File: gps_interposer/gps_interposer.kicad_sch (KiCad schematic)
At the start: 9 parts, among them J1 Module Connector, J2 Carrier Connector, J3 Conn_01x10, U1 SN74LVC1T45DBV, U2 SN74LVC1T45DBV

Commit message: PCB almost done.
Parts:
- removed J3: Conn_01x10, symbol Connector_Generic:Conn_01x10
- removed JP1: TXD, symbol Jumper:Jumper_2_Bridged
- added J3: Ext VSYS, Connector_PinHeader_2.54mm:PinHeader_1x02_P2.54mm_Horizontal, symbol Connector:Conn_01x02_Pin
- added J4: GENERIC_3V0, Connector_PinHeader_2.54mm:PinHeader_1x01_P2.54mm_Horizontal, symbol Connector_Generic:Conn_01x01
- added J6: GENERIC_3V3, Connector_PinHeader_2.54mm:PinHeader_1x01_P2.54mm_Horizontal, symbol Connector_Generic:Conn_01x01
- added JP1: TXD Direct, Connector_PinHeader_2.54mm:PinHeader_1x03_P2.54mm_Horizontal, symbol Jumper:Jumper_3_Bridged12
- added JP4: 3V3 Zero, Connector_PinHeader_2.54mm:PinHeader_1x02_P2.54mm_Horizontal, symbol Jumper:Jumper_2_Bridged
- added JP5: 1PPS Direct, Connector_PinHeader_2.54mm:PinHeader_1x02_P2.54mm_Horizontal, symbol Jumper:Jumper_2_Bridged
- added R10, R11, R17, R18, R20, R27, R3, R5, R7, R8: NC, Resistor_SMD:R_0603_1608Metric_Pad0.98x0.95mm_HandSolder, symbol Device:R
- added R12, R19, R21, R4, R6, R9: 1K, Resistor_SMD:R_0603_1608Metric_Pad0.98x0.95mm_HandSolder, symbol Device:R
- added R13, R14, R15, R16, R22, R23, R24, R25, R26: 0, Resistor_SMD:R_0603_1608Metric_Pad0.98x0.95mm_HandSolder, symbol Device:R
- added U3: RP20240-Zero, Kicad_Personal:RP2040-Zero, symbol Kicad_Personal:rp2040-zero
- added U4, U5, U6, U7: SN74LVC1T45DBV, Package_TO_SOT_SMD:SOT-23-6, symbol Logic_LevelTranslator:SN74LVC1T45DBV
- J1: footprint (none) -> Connector_PinSocket_1.27mm:PinSocket_2x05_P1.27mm_Vertical_SMD
- J2: value Carrier Connector -> Motherboard/Carrier Connector; footprint (none) -> Connector_PinHeader_1.27mm:PinHeader_2x05_P1.27mm_Vertical_SMD
- JP2: value Jumper_3_Bridged12 -> RXD Direct; footprint (none) -> Connector_PinHeader_2.54mm:PinHeader_1x03_P2.54mm_Horizontal
- R1, R2: value R -> NC; footprint (none) -> Resistor_SMD:R_0603_1608Metric_Pad0.98x0.95mm_HandSolder
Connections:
- net +3.3V: now also U2.6 (VCCB), JP4.1 (A), R8.2, U4.1 (VCCA), U5.6 (VCCB), U6.6 (VCCB), U7.6 (VCCB); no longer U2.1 (VCCA)
- net +3V0: now also U2.1 (VCCA), R11.2, R18.2, R21.2, R4.2, R5.2, U4.6 (VCCB), U5.1 (VCCA), U6.1 (VCCA), U7.1 (VCCA); no longer U2.6 (VCCB)
- net 1PPS_C: now also JP5.2 (B)
- net 1PPS_M: now also JP5.1 (A), R7.2, U4.4 (B)
- net ANT_BIAS_C: now also R25.2
- net ANT_BIAS_M: now also R25.1
- net BATT_C: now also R22.2
- net BATT_M: now also R22.1
- net GND: now also J3.1 (Pin_1), R12.1, R19.1, R27.1, R3.1, R6.1, R9.1, U3.22 (GND), U4.2 (GND), U5.2 (GND), U6.2 (GND), U7.2 (GND); no longer U1.5 (DIR), U2.5 (DIR)
- net RTCM_IN_C: now also R24.2
- net RTCM_IN_M: now also R24.1
- net RXD_C: now also JP2.2 (C), R20.2, U7.3 (A)
- net RXD_M_3V3: now also R13.2
- net TXD_C: now also JP1.2 (C)
- net TXD_M: now also U2.3 (A), JP1.1 (A); no longer U2.4 (B)
- net TXD_M_3V3: now also U2.4 (B), R14.2; no longer U2.3 (A)
- net RXD_M_3V0: now reaches JP2.3 (B), R2.1, U1.3 (A)
- net RSVD10 renamed RSVD10_C
- net RSVD10_C: now also R26.2; no longer J1.10 (Pin_10)
- net RSVD7 renamed RSVD7_C
- net RSVD7_C: now also R23.2; no longer J1.7 (Pin_7)
- new net: J4.1 (Pin_1), R17.1, U6.3 (A)
- new net: J6.1 (Pin_1), R17.2, U6.4 (B)
- new net: R21.1, R27.2, U7.5 (DIR)
- new net: R8.1, R9.2, U4.5 (DIR)
- new net: R13.1, U3.1 (GPIO0/SPI0_RX/I2C0_SDA/UART0_TX)
- new net: R14.1, U3.2 (GPIO1/SPI0_CSn/I2C0_SCL/UART0_RX)
- new net: JP4.2 (B), U3.21 (3V3)
- new net: J3.2 (Pin_2), U3.23 (VSYS)
- new net: R15.1, U3.5 (GPIO4/SPI0_RX_I2C0_SDA/UART1_TX)
- new net: R16.1, U3.6 (GPIO5/SPI0_CSn/I2C0_SCL/UART1_RX)
- new net: R5.1, R6.2, U1.5 (DIR)
- new net: R11.1, R12.2, U5.5 (DIR)
- new net: R3.2, R4.1, U2.5 (DIR)
- new net: R18.1, R19.2, U6.5 (DIR)
- new net 1PPS_M_3V3: R7.1, U3.3 (GPIO2/SPI0_SCLK/I2C1_SDA), U4.3 (A)
- new net RSVD10_M: J1.10 (Pin_10), R26.1
- new net RSVD7_M: J1.7 (Pin_7), R23.1
- new net RXD_C_3V3: R16.2, R20.1, U7.4 (B)
- new net TXD_C_3V0: JP1.3 (B), R10.1, U5.3 (A)
- new net TXD_C_3V3: R10.2, R15.2, U5.4 (B)
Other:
- note added: "---->"
- note added: "<----"
- note added: "DIR low -> B to A direction"
- moved on the sheet: J1, J2, JP2, R1, R2, U1

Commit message: PCB ready.
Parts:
- removed J4: GENERIC_3V0, Connector_PinHeader_2.54mm:PinHeader_1x01_P2.54mm_Horizontal, symbol Connector_Generic:Conn_01x01
- removed J6: GENERIC_3V3, Connector_PinHeader_2.54mm:PinHeader_1x01_P2.54mm_Horizontal, symbol Connector_Generic:Conn_01x01
- removed JP1: TXD Direct, Connector_PinHeader_2.54mm:PinHeader_1x03_P2.54mm_Horizontal, symbol Jumper:Jumper_3_Bridged12
- removed JP2: RXD Direct, Connector_PinHeader_2.54mm:PinHeader_1x03_P2.54mm_Horizontal, symbol Jumper:Jumper_3_Bridged12
- removed JP4: 3V3 Zero, Connector_PinHeader_2.54mm:PinHeader_1x02_P2.54mm_Horizontal, symbol Jumper:Jumper_2_Bridged
- removed JP5: 1PPS Direct, Connector_PinHeader_2.54mm:PinHeader_1x02_P2.54mm_Horizontal, symbol Jumper:Jumper_2_Bridged
- removed R17, R18: NC, Resistor_SMD:R_0603_1608Metric_Pad0.98x0.95mm_HandSolder, symbol Device:R
- removed R19: 1K, Resistor_SMD:R_0603_1608Metric_Pad0.98x0.95mm_HandSolder, symbol Device:R
- removed U6: SN74LVC1T45DBV, Package_TO_SOT_SMD:SOT-23-6, symbol Logic_LevelTranslator:SN74LVC1T45DBV
- added C1, C2, C4: 100n, Capacitor_SMD:C_0603_1608Metric_Pad1.08x0.95mm_HandSolder, symbol Device:C
- added H1, H2, H3, H4, H5, H6, H7, H8: MountingHole_Pad, Kicad_Personal:MountingHole_3.7mm_3.9mm_Pad_TopBottom, symbol Mechanical:MountingHole_Pad
- added R28, R30: NS, Resistor_SMD:R_0603_1608Metric_Pad0.98x0.95mm_HandSolder, symbol Device:R
- added R29, R31, R32, R33: 0, Resistor_SMD:R_0603_1608Metric_Pad0.98x0.95mm_HandSolder, symbol Device:R
- R2, R5: value NC -> NS
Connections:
- net +3.3V: now also R32.2
- net +3V0: now also C1.1, C2.1, C4.1
- net 1PPS_C: now also R33.2
- net 1PPS_M: now also R33.1
- net GND: now also C1.2, C2.2, C4.2, H1.1, H2.1, H3.1, H4.1, H5.1, H6.1, H7.1, H8.1
- net RXD_C: now also R29.2
- net RXD_M: now also R28.2, R29.1
- net RXD_M_3V0: now also R28.1
- net TXD_C: now also R30.2, R31.1
- net TXD_C_3V0: now also R30.1
- net TXD_M: now also R31.2
- net at U3.21 (3V3): now also R32.1

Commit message: PCB v2.
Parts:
- removed C1, C2, C4: 100n, Capacitor_SMD:C_0603_1608Metric_Pad1.08x0.95mm_HandSolder, symbol Device:C
- removed J3: Ext VSYS, Connector_PinHeader_2.54mm:PinHeader_1x02_P2.54mm_Horizontal, symbol Connector:Conn_01x02_Pin
- removed R1, R11, R20, R27, R3, R8: NC, Resistor_SMD:R_0603_1608Metric_Pad0.98x0.95mm_HandSolder, symbol Device:R
- removed R12, R21, R4, R6, R9: 1K, Resistor_SMD:R_0603_1608Metric_Pad0.98x0.95mm_HandSolder, symbol Device:R
- removed R22, R23, R24, R25, R26, R32, R33: 0, Resistor_SMD:R_0603_1608Metric_Pad0.98x0.95mm_HandSolder, symbol Device:R
- removed R28, R30, R5: NS, Resistor_SMD:R_0603_1608Metric_Pad0.98x0.95mm_HandSolder, symbol Device:R
- removed U1, U2, U4, U5, U7: SN74LVC1T45DBV, Package_TO_SOT_SMD:SOT-23-6, symbol Logic_LevelTranslator:SN74LVC1T45DBV
- added J5: Conn_01x04_Pin, Connector_PinHeader_2.54mm:PinHeader_1x04_P2.54mm_Horizontal, symbol Connector:Conn_01x04_Pin
- added R17, R18, R19: 9k, Resistor_SMD:R_0603_1608Metric_Pad0.98x0.95mm_HandSolder, symbol Device:R
- H1, H2, H3, H4, H5, H6, H7, H8: footprint Kicad_Personal:MountingHole_3.7mm_3.9mm_Pad_TopBottom -> Kicad_Personal:MountingHole_2.5mm_3.9mm_Pad_TopBottom_1
- R10: value NC -> 1k
- R13, R16, R31: now not fitted; now left out of the parts list
- R2: value NS -> 1k; now not fitted; now left out of the parts list
- R7: value NC -> 1k; now not fitted; now left out of the parts list
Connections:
- net ANT_BIAS_M is gone; now on net ANT_BIAS_C: J1.9 (Pin_9)
- net BATT_M is gone; now on net BATT_C: J1.6 (Pin_6)
- net RSVD10_M is gone; now on net RSVD10_C: J1.10 (Pin_10)
- net RSVD7_M is gone; now on net RSVD7_C: J1.7 (Pin_7)
- net RTCM_IN_M is gone; now on net RTCM_IN_C: J1.8 (Pin_8)
- net RXD_C_3V3 is gone; now on net RXD_C: R16.2
- net RXD_M_3V0 is gone; now on net RXD_M_3V3: R2.1
- net TXD_C_3V0 is gone; now on net TXD_C: R10.1
- net TXD_M_3V3 is gone; now on net TXD_M: R14.2
- net +3.3V: now also U3.21 (3V3), J5.2 (Pin_2)
- net +3V0: now also J5.1 (Pin_1)
- net 1PPS_C: now also J1.4 (Pin_4), R7.1
- net 1PPS_M_3V3: now also R7.2, R17.2; no longer R7.1
- net GND: now also J5.4 (Pin_4), R17.1, R18.1, R19.1
- net RTCM_IN_C: now also U3.10 (GPIO9/SPI1_CSn/I2C0_SCL/UART1_RX)
- net RXD_M: now also R2.2, R18.2
- net RXD_M_3V3: no longer R2.2
- net TXD_C: now also R19.2
- net VSYS: now reaches U3.23 (VSYS)
- net VSYS: now also J5.3 (Pin_3)
- removed net 1PPS_M: J1.4 (Pin_4), R7.2
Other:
- moved on the sheet: R10

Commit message: Additional connectors.
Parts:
- added J3: Conn_01x05, Connector_PinHeader_2.54mm:PinHeader_1x05_P2.54mm_Vertical_SMD_Pin1Left, symbol Connector_Generic:Conn_01x05
- added J4: Conn_01x04, Connector_PinHeader_2.54mm:PinHeader_1x04_P2.54mm_Horizontal, symbol Connector_Generic:Conn_01x04
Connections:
- net +3.3V: now also J4.1 (Pin_1)
- net 1PPS_C: now also J3.4 (Pin_4)
- net GND: now also J3.5 (Pin_5), J4.4 (Pin_4)
- net RXD_M: now also J3.1 (Pin_1)
- net TXD_C: now also J3.3 (Pin_3)
- net TXD_M: now also J3.2 (Pin_2)
- net VSYS: now also J4.2 (Pin_2)

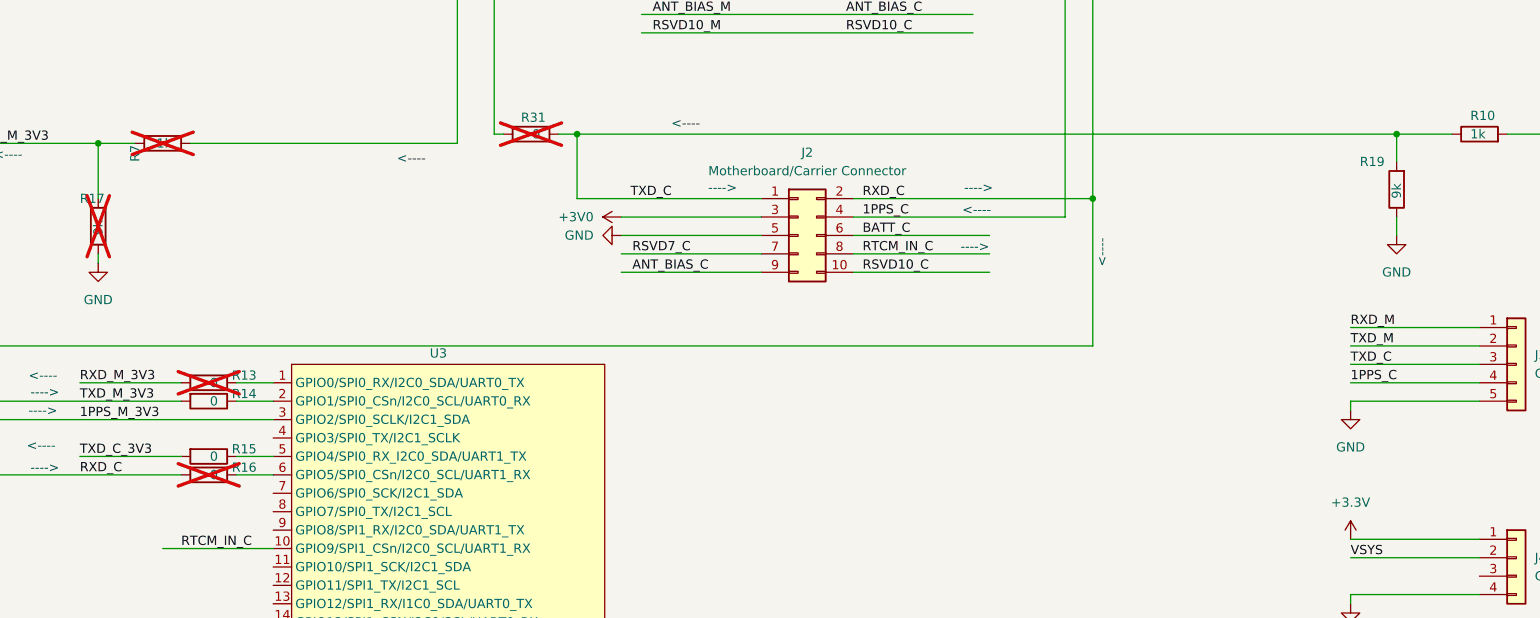
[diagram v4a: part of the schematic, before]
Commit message: Blink LED. Mark correct resistors as installed.
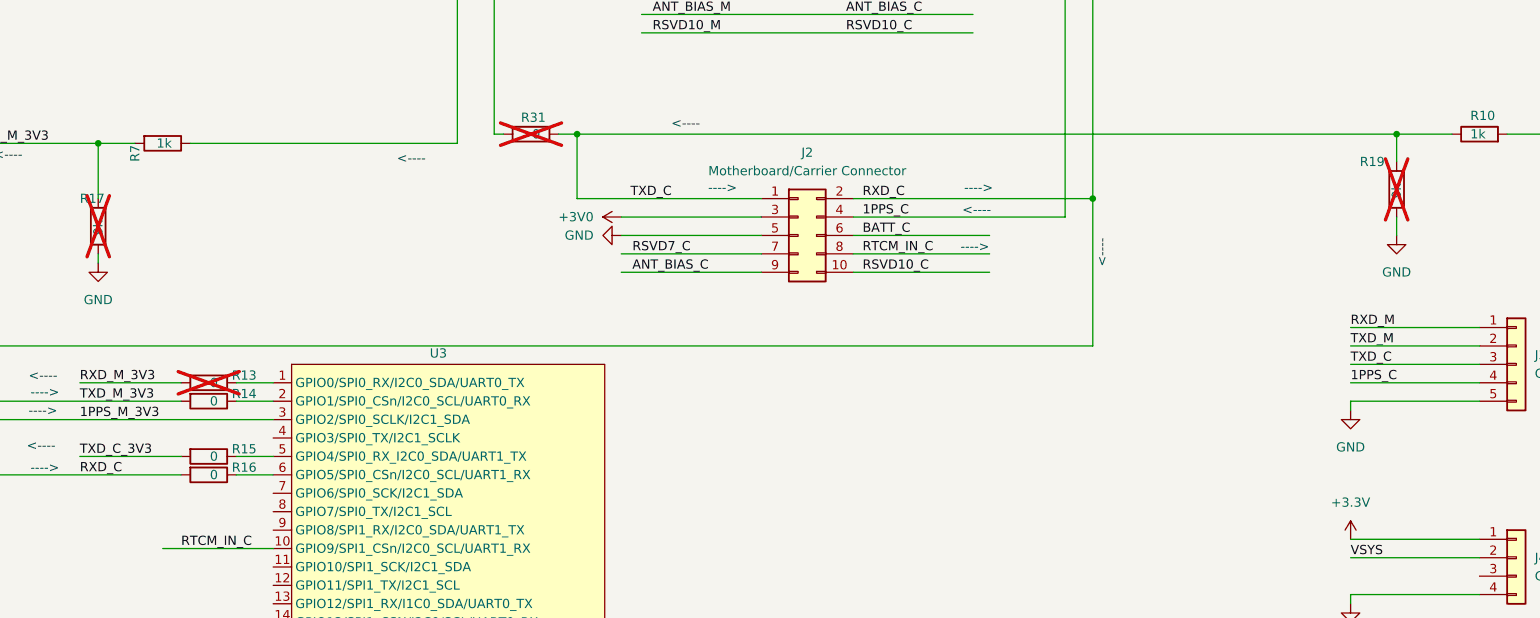
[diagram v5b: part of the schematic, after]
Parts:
- R16, R7: now fitted; now in the parts list
- R19: now not fitted; now left out of the parts list
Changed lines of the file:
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@@
 		(unit 1)
 		(exclude_from_sim no)
-		(in_bom no)
-		(on_board yes)
-		(dnp yes)
+		(in_bom yes)
+		(on_board yes)
+		(dnp no)
 		(property "Reference" "R7"
 			(at 48.26 95.25 0)
@@
 		(unit 1)
 		(exclude_from_sim no)
-		(in_bom yes)
-		(on_board yes)
-		(dnp no)
+		(in_bom no)
+		(on_board yes)
+		(dnp yes)
 		(property "Reference" "R19"
 			(at 217.17 95.25 0)
@@
 		(unit 1)
 		(exclude_from_sim no)
-		(in_bom no)
-		(on_board yes)
-		(dnp yes)
+		(in_bom yes)
+		(on_board yes)
+		(dnp no)
 		(property "Reference" "R16"
 			(at 65.024 137.414 90)

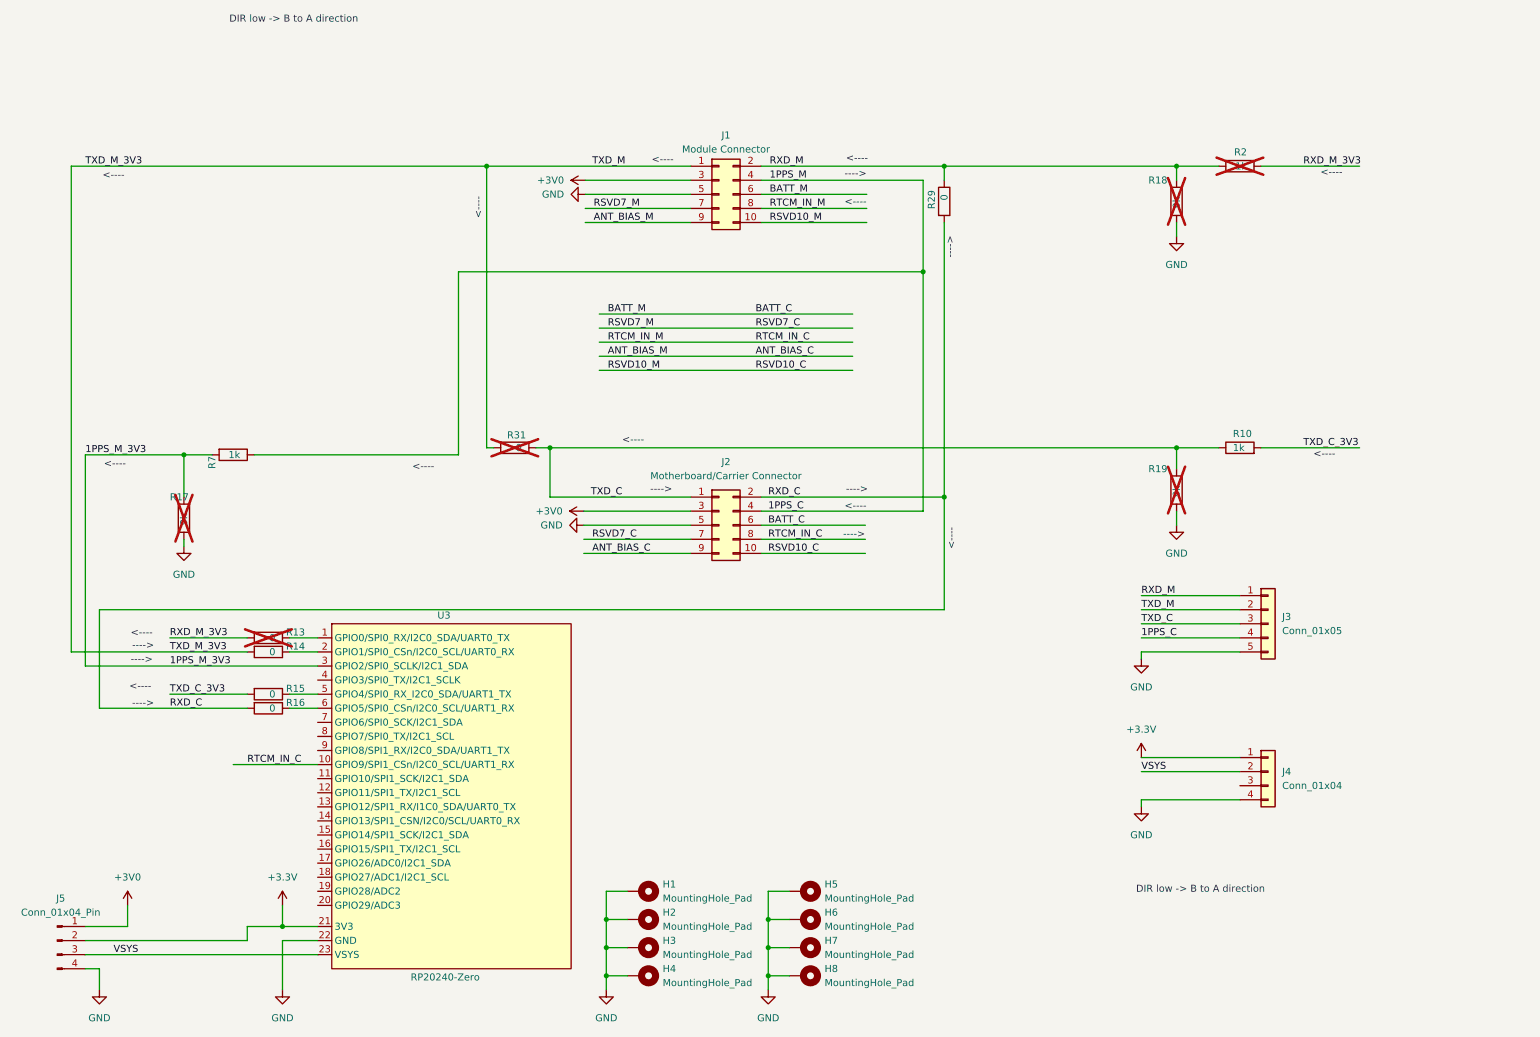
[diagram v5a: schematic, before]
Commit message: Wire up RX interposer.
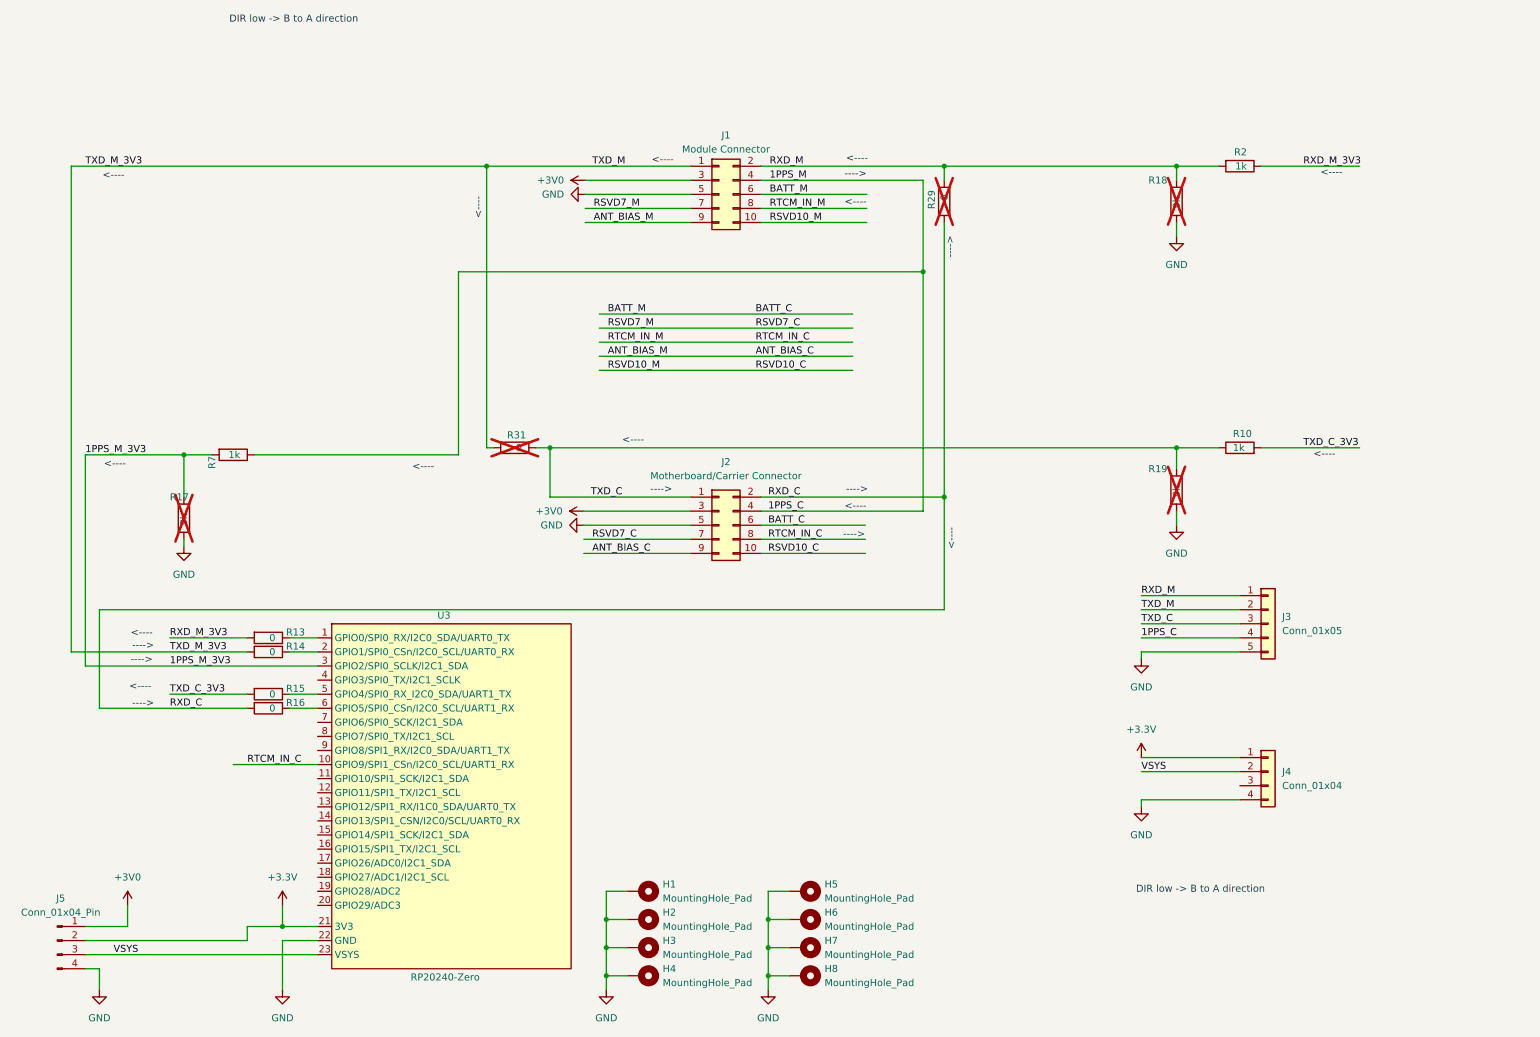
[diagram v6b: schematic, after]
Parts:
- R13, R2: now fitted; now in the parts list
- R29: now not fitted; now left out of the parts list
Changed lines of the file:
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@@
 		(unit 1)
 		(exclude_from_sim no)
-		(in_bom no)
-		(on_board yes)
-		(dnp yes)
+		(in_bom yes)
+		(on_board yes)
+		(dnp no)
 		(property "Reference" "R13"
 			(at 65.024 124.714 90)
@@
 		(unit 1)
 		(exclude_from_sim no)
-		(in_bom yes)
-		(on_board yes)
-		(dnp no)
+		(in_bom no)
+		(on_board yes)
+		(dnp yes)
 		(property "Reference" "R29"
 			(at 178.054 44.958 90)
@@
 		(unit 1)
 		(exclude_from_sim no)
-		(in_bom no)
-		(on_board yes)
-		(dnp yes)
+		(in_bom yes)
+		(on_board yes)
+		(dnp no)
 		(property "Reference" "R2"
 			(at 234.95 38.1 90)
